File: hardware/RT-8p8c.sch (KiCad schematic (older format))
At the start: 43 parts, among them J1 SI-60062-F, P1 , P2 , P3 ICSP, P4 , U1 PIC32MX764F128H, U2 KSZ8051MLL, U3 LP2985LV, X1 8Mhz, X2 25MHz

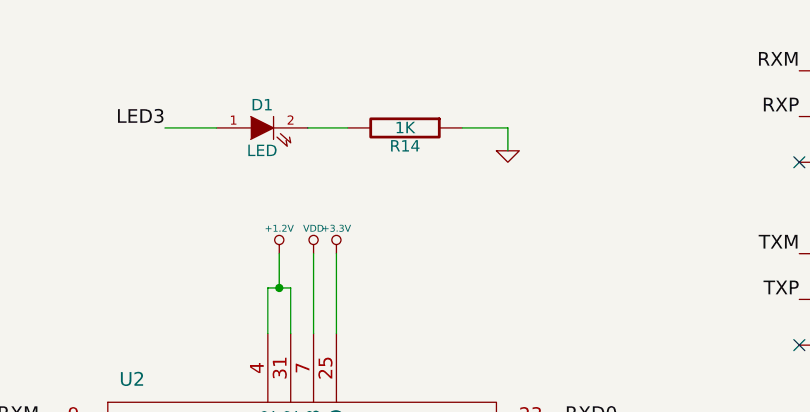
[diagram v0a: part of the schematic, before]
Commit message: change component sizes and value
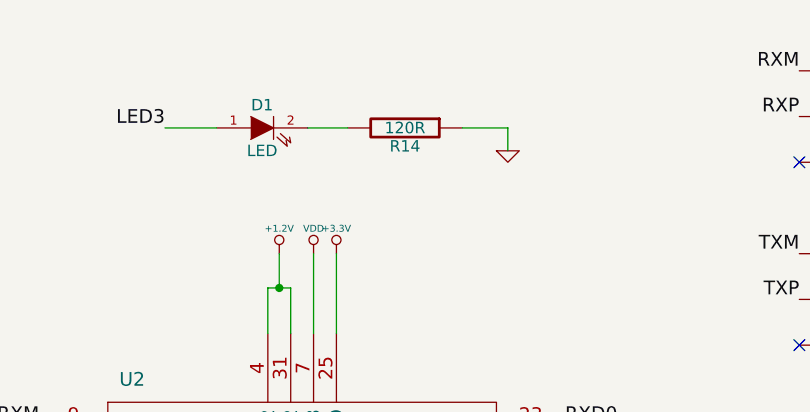
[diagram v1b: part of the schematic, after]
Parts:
- R14: value 1K -> 120R
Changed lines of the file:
@@
-EESchema Schematic File Version 2  date Monday 23,July,2012 01:23:55 PM SGT
+EESchema Schematic File Version 2  date Tuesday 24,July,2012 09:15:29 AM SGT
 LIBS:power
 LIBS:device
@@
 LIBS:contrib
 LIBS:valves
-LIBS:mine
 LIBS:RT-8p8c-cache
 EELAYER 25  0
@@
 Sheet 1 1
 Title "RT-8p8c Module"
-Date "23 jul 2012"
+Date "24 jul 2012"
 Rev "A.1"
 Comp ""
@@
 P 6800 1250
 F 0 "R14" V 6880 1250 50  0000 C CNN
-F 1 "1K" V 6800 1250 50  0000 C CNN
+F 1 "120R" V 6800 1250 50  0000 C CNN
 	1    6800 1250
 	0    1    1    0

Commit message: routing issue
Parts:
- added P5, P6: (no value), symbol CONN_1
- added R1: 1K, symbol R
- added R15: 220R, symbol R
- R14: value 120R -> 220R
- R16: renamed from R1; value 1K -> 220R
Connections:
- net +3.3V: now also J1.11 (LA), J1.13 (RA), P1.18
- net GND: now also P6.1; no longer J1.12 (LC), J1.14 (RC), P1.18, R16.1
- net LED0: now also R15.2; no longer J1.11 (LA)
- net LED1: now also R16.2; no longer J1.13 (RA)
- net PWM_D renamed PWMD
- removed net RST: R16.2, U1.48 (SOSCO/T1CK/CN0/RC14), U2.47 (RST)
- new net: J1.12 (LC), R16.1
- new net: R1.1, U1.48 (SOSCO/T1CK/CN0/RC14)
- new net: J1.14 (RC), R15.1
- new net PHYRST: P5.1, R1.2, U2.47 (RST)
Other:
- moved on the sheet: D1, R10, R11, R12, R14, R16, R2, R3, R4, R5, R6, R7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
